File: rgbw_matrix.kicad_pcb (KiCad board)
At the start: 2 copper layers, 48 x 72 mm, 47 parts, among them IC1 TLC59283DBQR, IC2 TLC59283DBQR, IC3 TLC59283DBQR, IC4 TLC59283DBQR, IC5 TLC59283DBQR, IC6 TLC59283DBQR, J1 Conn_01x07_Female

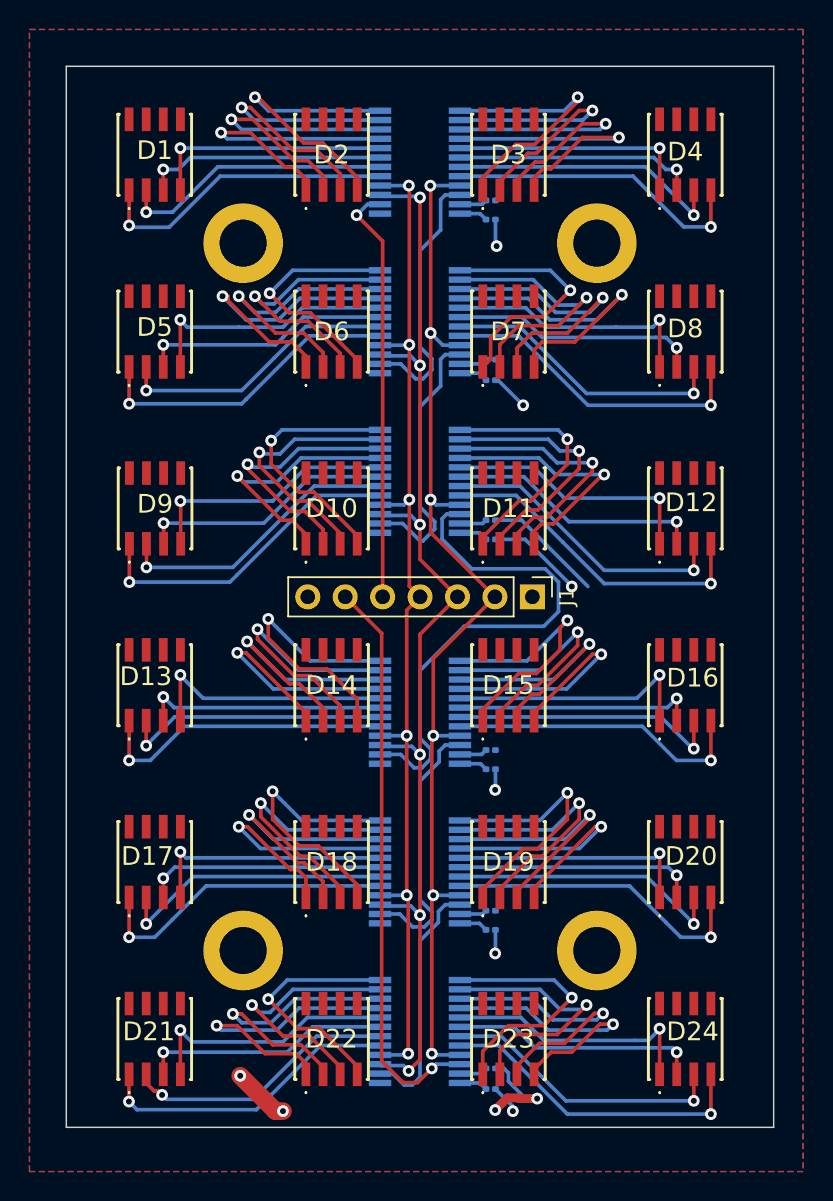
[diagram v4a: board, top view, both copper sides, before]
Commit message: capacitors fixed
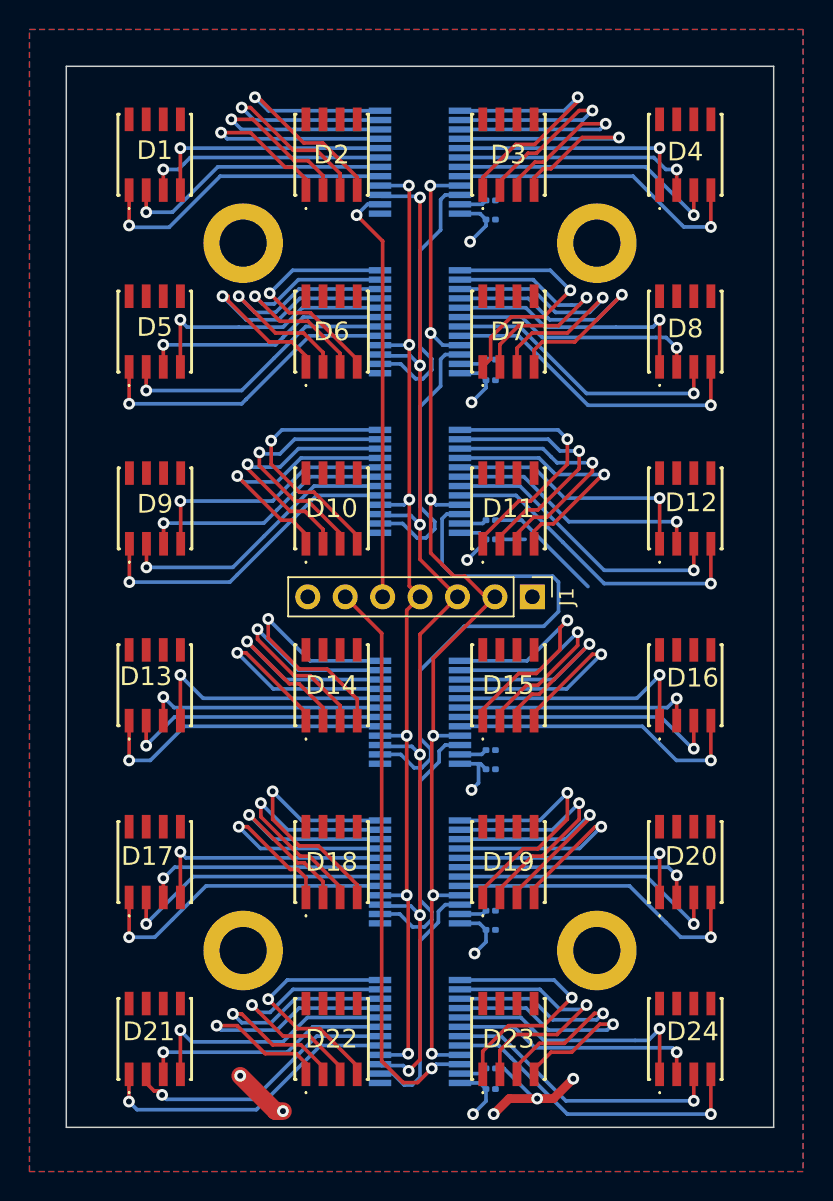
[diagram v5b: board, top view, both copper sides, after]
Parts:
- turned C1 to 180 degrees
- turned C2 to 180 degrees
- turned C3 to 180 degrees
- turned C5 to 180 degrees
- turned C6 to 180 degrees
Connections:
- C1 pad 1: Net-(C1-Pad1) -> GND
- C2 pad 1: Net-(C2-Pad1) -> GND
- C3 pad 1: Net-(C3-Pad1) -> GND
- C4 pad 1: Net-(C4-Pad1) -> VCC
- C4 pad 2: VCC -> GND
- C5 pad 1: Net-(C5-Pad1) -> GND
- C6 pad 1: Net-(C6-Pad1) -> GND
- IC1 pad 24: Net-(C1-Pad1) -> VCC
- IC2 pad 24: Net-(C2-Pad1) -> VCC
- IC3 pad 24: Net-(C3-Pad1) -> VCC
- IC4 pad 24: Net-(C4-Pad1) -> VCC
- IC5 pad 24: Net-(C5-Pad1) -> VCC
- IC6 pad 24: Net-(C6-Pad1) -> VCC
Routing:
- net VCC: track 15.9 -> 23.4 mm
- net GND: track 18.3 -> 24.1 mm, vias 4 -> 5
- net Net-(C2-Pad1): track 1.96 -> 0.00 mm
- net Net-(C3-Pad1): track 1.95 -> 0.00 mm
- net Net-(C5-Pad1): track 1.95 -> 0.00 mm
- net Net-(C6-Pad1): track 1.94 -> 0.00 mm
- net Net-(C1-Pad1): track 1.93 -> 0.00 mm
- net Net-(C4-Pad1): track 1.92 -> 0.00 mm
- net Net-(IC3-Pad22): track 35.2 -> 36.3 mm
- net BLANK: track 74.5 -> 75.3 mm

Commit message: added silkscreen text
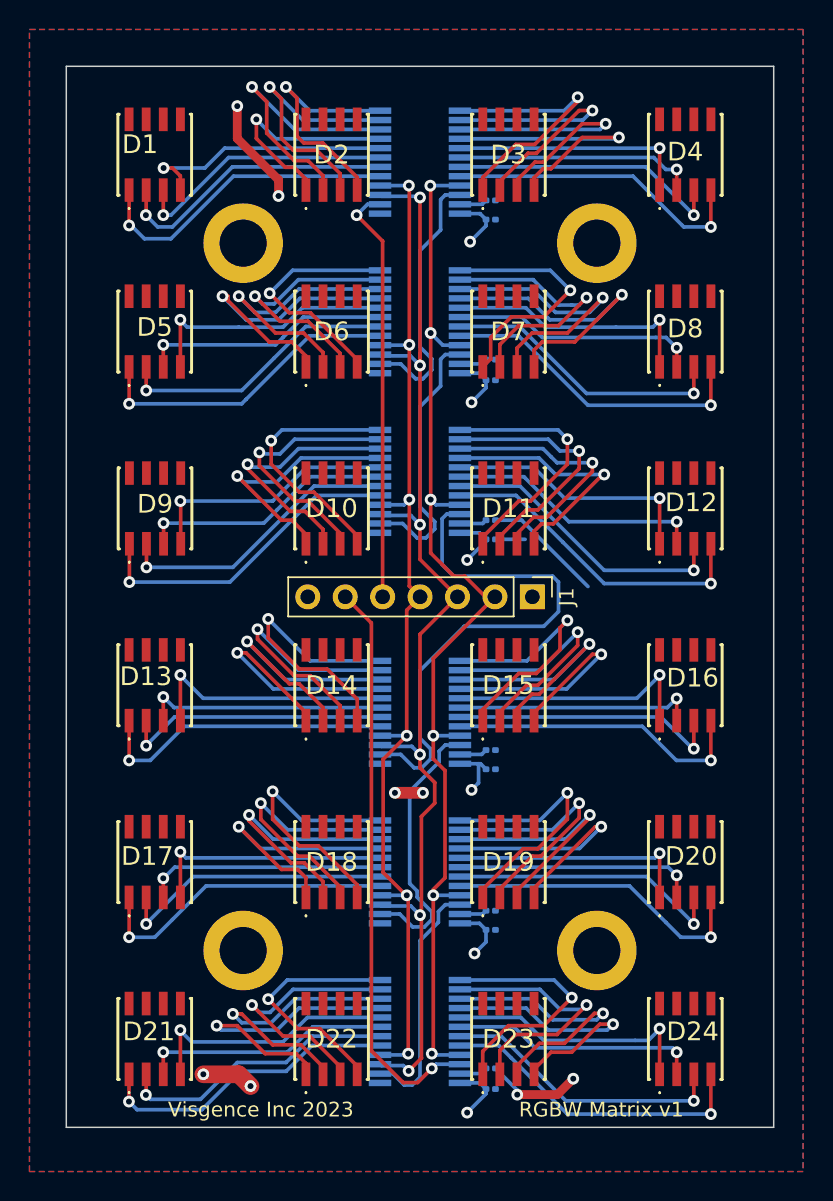
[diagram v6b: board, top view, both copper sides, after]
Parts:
- added G: LOGO, local:LOGO_SMALL, B.Cu at (32.7, 28.9)
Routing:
- net GND: track 24.1 -> 29.5 mm, vias 5 -> 8
- net D2W: track 18.8 -> 15.5 mm
- net D2R: track 18.9 -> 16.8 mm
- net D1G: track 16.4 -> 18.0 mm
- net LAT: track 71.5 -> 72.8 mm
- net D1R: track 16.4 -> 17.6 mm
- net D2G: track 19.4 -> 18.3 mm
- net D1B: track 18.6 -> 19.6 mm
- net SCLK: track 79.3 -> 80.1 mm
- net BLANK: track 75.3 -> 76.0 mm
- net D1W: track 20.8 -> 21.4 mm
- net Net-(IC4-Pad22): track 18.0 -> 18.5 mm
- net D21B: track 18.7 -> 19.2 mm
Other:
- board text added: "RGBW Matrix v1"
- board text added: "Visgence Inc 2023"

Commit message: track and via improment
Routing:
- net GND: track 29.5 -> 39.8 mm, vias 8 -> 9
- net D23R: track 18.1 -> 21.3 mm
- net D15G: track 17.3 -> 19.9 mm
- net D15R: track 17.3 -> 19.9 mm
- net SCLK: track 80.1 -> 78.0 mm
- net D15B: track 17.7 -> 19.7 mm
- net D23G: track 18.4 -> 20.3 mm
- net D3W: track 18.1 -> 19.9 mm
- net Net-(IC4-Pad22): track 18.5 -> 16.8 mm
- net D14W: track 17.6 -> 19.3 mm
- net D3B: track 18.1 -> 19.7 mm
- net D15W: track 18.3 -> 19.7 mm
- net D22W: track 19.7 -> 21.1 mm
- net D3G: track 18.3 -> 19.6 mm
- net LAT: track 72.8 -> 74.0 mm
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
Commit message: via and track realignment
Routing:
- net D15W: track 19.7 -> 18.7 mm
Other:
- board text added: "BLNK"
- board text added: "GND"
- board text added: "LAT"
- board text added: "SCLK"
- board text added: "SIN"
- board text added: "SOUT"
- board text added: "VCC"
